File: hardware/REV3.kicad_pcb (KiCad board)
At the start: 4 copper layers, 36.9 x 36.9 mm, 111 parts, among them J1 USB_C_Receptacle_USB2.0_14P, J2 Conn_01x08, Q1 2N7002, SW1 SW_Push, U1 STM32F405RGT6, U1_RX ELRS, U1_TX ELRS, U2 USBLC6-2SC6, U2_RX GPS, U2_TX GPS, U3 DPS310, U3_RX VTX, U3_TX VTX, U4 AP2112K-3.3, U5 W25Q128JVP, U5_TX Conn_01x01_Pin, U6 LMR51635XDDCR, U8 AT7456, Y1 8MHz, Y2 27MHZ

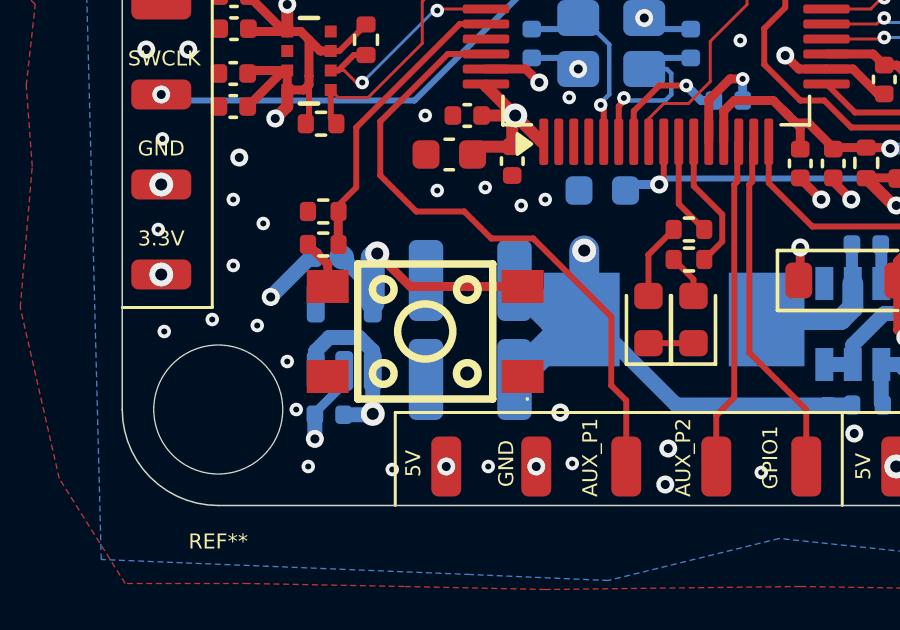
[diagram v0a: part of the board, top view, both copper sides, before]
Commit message: Update PCB layout, top copper render, and add vector schematic
Bring in the updated REV3.kicad_pcb and its regenerated top copper
render from the latest project export, and add the schematic as an
SVG (SCHEMATIC_SVG/REV3.svg) alongside the existing PDF, using the
SVG for the inline README preview since it scales cleanly.

Co-Authored-By: Claude Sonnet 5 <noreply@anthropic.com>
Claude-Session: https://claude.ai/code/session_01NcYZJYs4sXtJCwSdQYcunV
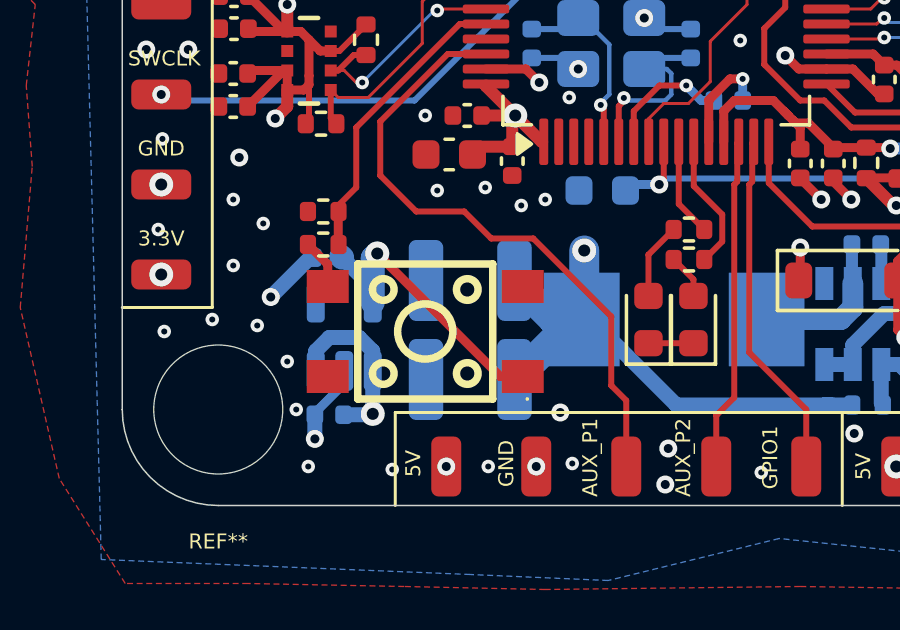
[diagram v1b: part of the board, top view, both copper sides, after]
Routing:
- net +3.3V: track 50.6 -> 51.8 mm
